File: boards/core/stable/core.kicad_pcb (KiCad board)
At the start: 2 copper layers, 215 x 100 mm, 361 parts, among them J201 Conn_02x08_Counter_Clockwise, J202 Conn_02x08_Counter_Clockwise, J203 Conn_02x08_Counter_Clockwise, J204 Conn_02x08_Counter_Clockwise, J207 Screw_Terminal_01x03, J214 Conn_02x04_Counter_Clockwise, Q201 2N3906, Q202 BC847BS, Q203 MMBFJ111, Q204 2N3906, Q205 BC847BS, Q206 MMBFJ111, Q207 BC847BS, Q208 BC548C, Q209 BC548C, Q210 BC548C, Q211 J111, Q212 MMBT5551, Q213 MMBT5551, Q214 MMBT5551, Q215 J111, U201 TL072, U202 TL072, U203 LM311, U204 TL072, U205 TL072, U206 LM311, U207 TL072, U208 TL072, U209 TL072, U210 TL072, U211 TL072, U212 4002, U213 LM358, U214 TL072, U215 CD4053B, U216 NE5532, U217 TL072, U218 TL072, U219 TL072, U220 TL072, U221 TL072, U222 TL072, U223 TL072, U225 TL072, U226 TL072, U227 TL072, U228 CD4040BM96

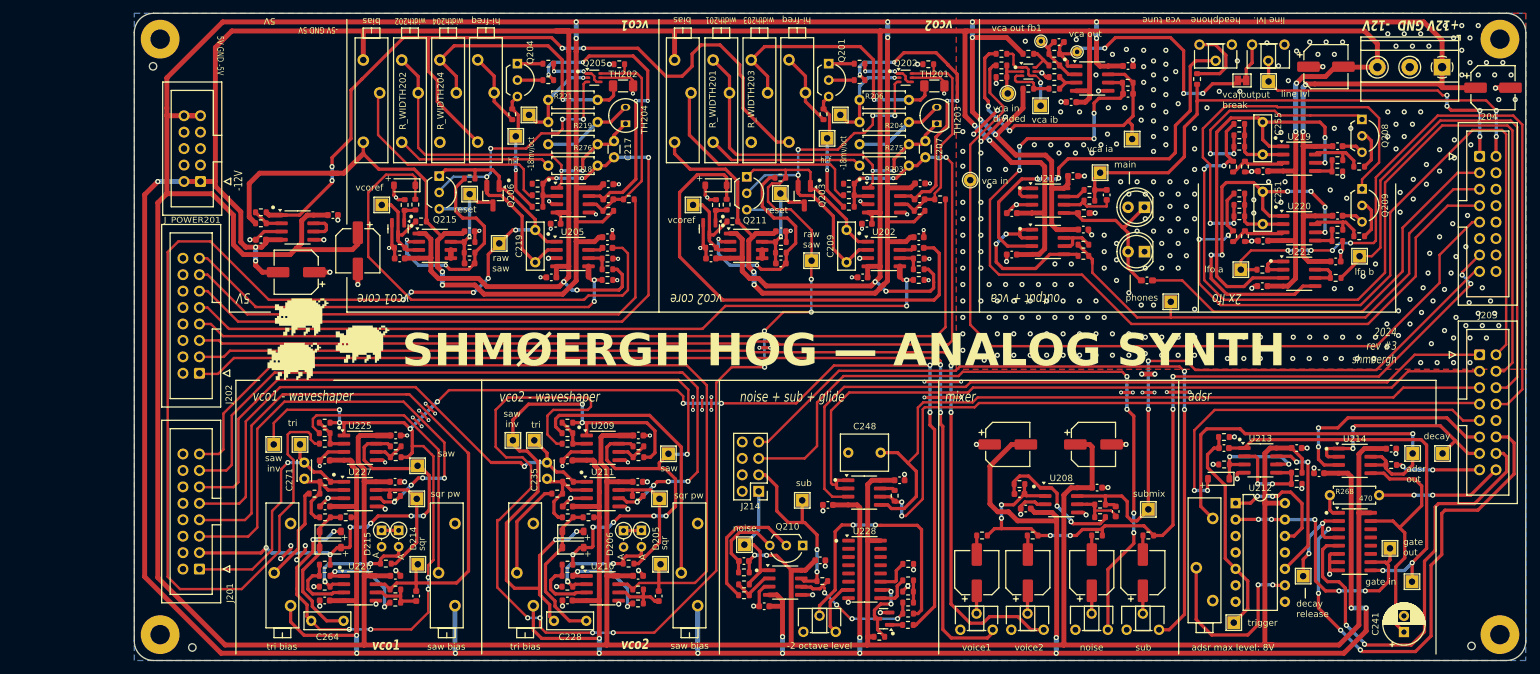
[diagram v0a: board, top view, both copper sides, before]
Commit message: Streamline 'Stable' Core board
https://github.com/shmoergh/hog/issues/7

- Remove 12V terminal input
- Reposition Eurorack power connector to right so it makes space for tuning
- Remove all unnecessary thermal compensation pseudo components
- Reposition tuning trimmers
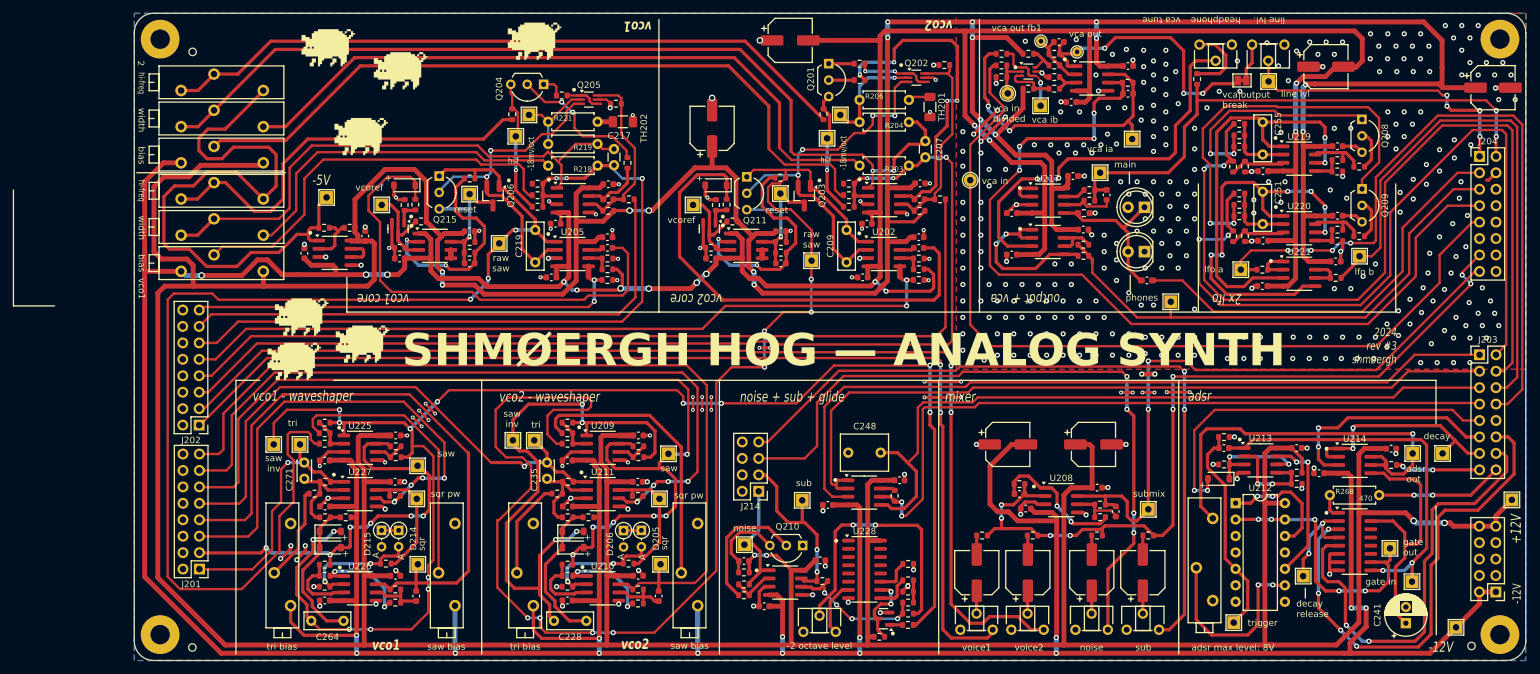
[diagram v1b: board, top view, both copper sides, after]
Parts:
- removed J207: Screw_Terminal_01x03, TerminalBlock_Phoenix:TerminalBlock_Phoenix_MKDS-1,5-3_1x03_P5.00mm_Horizontal
- removed R275, R276: See t.comp. table, Shmoergh_Custom_Footprints:R_Axial_DIN0207_L6.3mm_D2.5mm_P7.62mm_Horizontal
- removed R_WIDTH203, R_WIDTH204: See t.comp. table, Potentiometer_THT:Potentiometer_Bourns_3006P_Horizontal
- removed TH203, TH204: See t.comp. table, Package_TO_SOT_THT:TO-92-2
- added G***: LOGO, Shmoergh_Custom_Footprints:Gyeszno, F.Cu at (59.0, 168.3)
- added G***: LOGO, Shmoergh_Custom_Footprints:Gyeszno, F.Cu at (70.1, 171.9)
- added G***: LOGO, Shmoergh_Custom_Footprints:Gyeszno, F.Cu at (64.1, 182.1)
- added G***: LOGO, Shmoergh_Custom_Footprints:Gyeszno, F.Cu at (90.8, 167.3)
- added TP235: 12V, TestPoint:TestPoint_THTPad_2.0x2.0mm_Drill1.0mm, F.Cu at (241.9, 238.2)
- added TP236: -12V, TestPoint:TestPoint_THTPad_2.0x2.0mm_Drill1.0mm, F.Cu at (233.2, 257.9)
- added TP237: -5V, TestPoint:TestPoint_THTPad_2.0x2.0mm_Drill1.0mm, F.Cu at (58.7, 191.4)
- J201, J202, J203, J204: footprint Connector_IDC:IDC-Header_2x08_P2.54mm_Vertical -> Connector_PinHeader_2.54mm:PinHeader_2x08_P2.54mm_Vertical
- J_POWER201: footprint Connector_IDC:IDC-Header_2x05_P2.54mm_Vertical -> Connector_PinHeader_2.54mm:PinHeader_2x05_P2.54mm_Vertical
- Q202, Q205: footprint Package_TO_SOT_SMD:SOT-363_SC-70-6 -> Package_TO_SOT_SMD:SOT-363_SC-70-6_Handsoldering
- R203, R218: value See t.comp. table -> 91k
- R204, R219: value See t.comp. table -> 6.2k (50ppm)
- R206, R221: value See t.comp. table -> 4R22 (50ppm)
- R_WIDTH201, R_WIDTH202: value See t.comp. table -> 20k
- moved J_POWER201 209.9 mm to (239.4, 252.4)
- moved C256 84.3 mm to (130.3, 167.2), turned to 0 degrees
- moved R_HIFREQ201 81.6 mm to (48.9, 174.9), turned to 0 degrees
- moved R_WIDTH201 69.5 mm to (48.9, 180.5), turned to 0 degrees
- moved R_BIAS203 63.6 mm to (48.9, 186.1), turned to 0 degrees
- moved C252 57.9 mm to (118.3, 180.8), turned to 90 degrees
- moved R_HIFREQ202 34.3 mm to (48.9, 191.7), turned to 0 degrees
- moved R_WIDTH202 25.8 mm to (48.9, 197.3), turned to 0 degrees
- moved R_BIAS201 25.2 mm to (48.9, 202.9), turned to 0 degrees
- moved R222 17.7 mm to (105.2, 186.1), turned to 90 degrees
- moved R300 13.7 mm to (62.3, 196.1), turned to 180 degrees
- moved R301 10.1 mm to (58.3, 196.1), turned to 180 degrees
- moved J202 8.00 mm to (39.0, 226.6)
- moved C263 7.04 mm to (55.3, 200.1), turned to -90 degrees
- moved U223 6.97 mm to (60.0, 200.0)
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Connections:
- R204 pad 1: Net-(R204-Pad1) -> Net-(C207-Pad2)
- R219 pad 1: Net-(R219-Pad1) -> Net-(C217-Pad2)
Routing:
- net +12V: track 1191.4 -> 1063.9 mm, vias 18 -> 20
- net Net-(R210-Pad2): track 11.5 -> 107.4 mm
- net -12V: track 1064.5 -> 974.3 mm, vias 25 -> 29
- net Net-(C207-Pad2): track 56.2 -> 143.4 mm
- net Net-(R203-Pad2): track 24.1 -> 107.5 mm
- net Net-(R318-Pad1): track 36.2 -> 116.4 mm
- net Net-(R225-Pad2): track 11.5 -> 63.1 mm
- net Net-(R221-Pad2): track 42.7 -> 2.37 mm, vias 1 -> 0
- net Net-(R206-Pad2): track 42.6 -> 3.44 mm, vias 1 -> 0
- net Net-(C218-Pad2): track 46.7 -> 9.47 mm, vias 4 -> 0
- net -5V: track 133.7 -> 98.1 mm, vias 4 -> 0
- net Net-(R218-Pad2): track 24.1 -> 53.5 mm
- net Net-(C217-Pad2): track 56.2 -> 83.9 mm, vias 2 -> 0
- net Net-(R319-Pad1): track 36.2 -> 62.7 mm
- net GND: track 232.5 -> 212.6 mm, vias 405 -> 419
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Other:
- board text added: "-5V"
- board text added: "2"
- board text added: "width"
- board text removed: "-5V GND 5V"
- board text removed: "12V"
- board text removed: "202width"
- board text removed: "204width"
- board text removed: "5V"
- board text removed: "5V GND -5V"
- board text removed: "all shield GNDs don't connect them on the other end!"
- board text removed: "width201"
- board text removed: "width202"
- board text removed: "width203"
- board text removed: "width204"

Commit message: Repositioned connectors on Core board
ref https://github.com/shmoergh/hog/issues/30

Connectors have to be aligned on the 1mm grid on the Core board so that it's easy to align the connector pairs on the UI board.
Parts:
- moved TP236 21.4 mm to (242.0, 238.3)
- moved TP235 17.8 mm to (233.0, 253.6)
- moved J_POWER201 10.7 mm to (237.0, 242.0), turned to 0 degrees
- moved J202 0.63 mm to (39.0, 226.0)
- moved J203 0.28 mm to (237.0, 216.0)
- moved J204 0.18 mm to (237.0, 185.0)
- moved J201 0.14 mm to (39.0, 249.0)
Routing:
- net -12V: track 974.3 -> 997.3 mm
- net +12V: track 1063.9 -> 1071.3 mm
- net GLIDED_PITCH: track 110.5 -> 111.1 mm
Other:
- board text added: "* All mounting holes"
- board text added: "Board dimensions: 215x100mm Through hole components: [TK]"
- board text removed: "Case dimensions: 342x240mm Board dimensions: 215x100mm Through hole components: 63"

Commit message: Updated and checked Core board BOM
ref https://github.com/shmoergh/hog/issues/19
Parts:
- RV201, RV202, RV203, RV204, RV205: value 100k Log -> 100k
- TH201, TH202: value PTS120602B100RP100 -> PTS120601B100RP100
